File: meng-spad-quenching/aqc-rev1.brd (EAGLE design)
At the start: 127 x 88.9 mm, 137 parts, among them IC1 ADCMP582, IC2 NC7SV74K8X, IC3 LT3032-5, IC4 OPA342, IC5 OPA342, IC6 LTC1711, IC7 DS1100LU-20+, IC8 LT3032-15, IC9 NC7WZ16P6X, J1 VIN_LOGIC, M1 BSS806N, Q1 MMBTH81, Q2 MMBTH81, Q3 MMBTH81, Q4 MMBTH81, Q5 MMBTH81, Q6 MMBTH81, T1 MMBTH10, T2 MMBTH10, T3 MMBTH10, T4 MMBTH10, T5 MMBTH10, T6 MMBTH10, T7 MMBTH10, U1 SN65EPT21DGK, U2 TPS78233DDCT, U3 SN65EPT22DGK, X1 CONN_SPAD, X2 CONN_PHOTON_COUNTER, X3 CONN_FORCE_QUENCH, X4 CONN_VREF_ONE_SHOT_EXT, X5 CONN_VREF_DIAMOND_IBIAS_EXT, X6 CONN_VREF_CASCODE_IBIAS_EXT

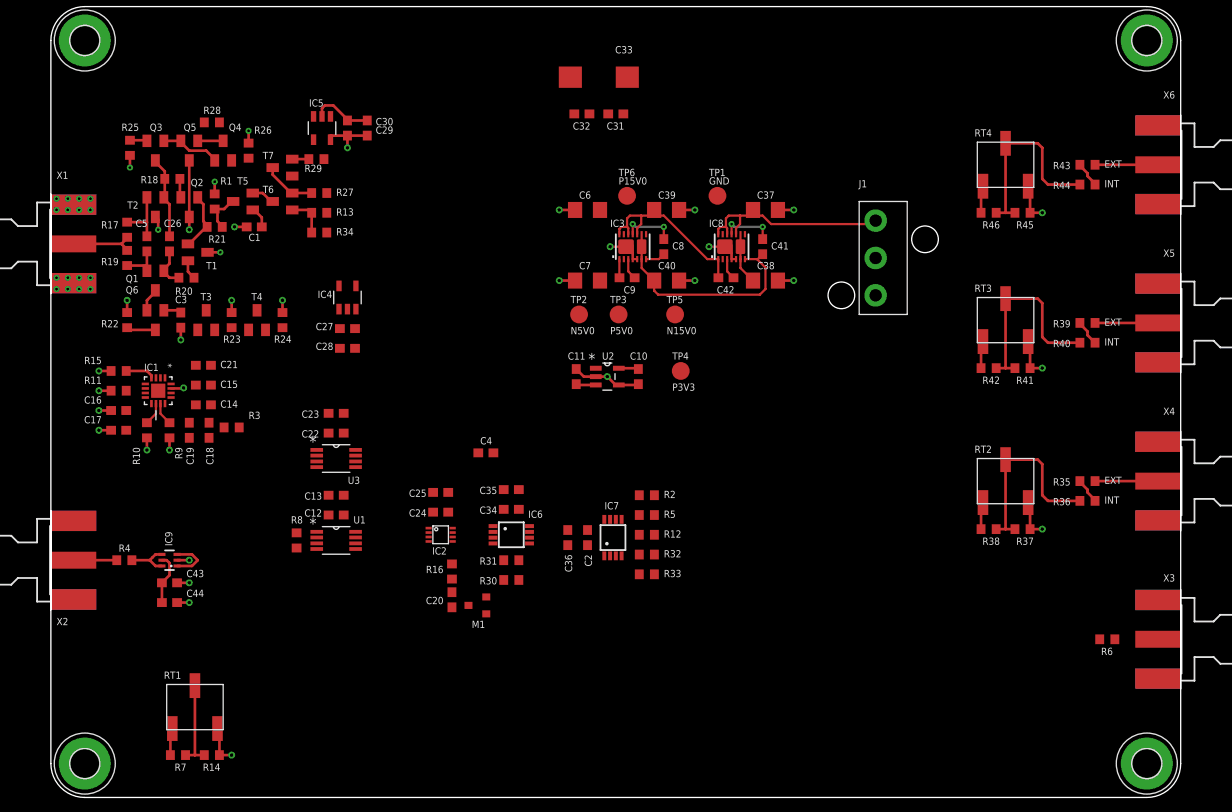
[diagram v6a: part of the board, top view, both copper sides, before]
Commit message: Worked on layout of CCS in AQC output stage
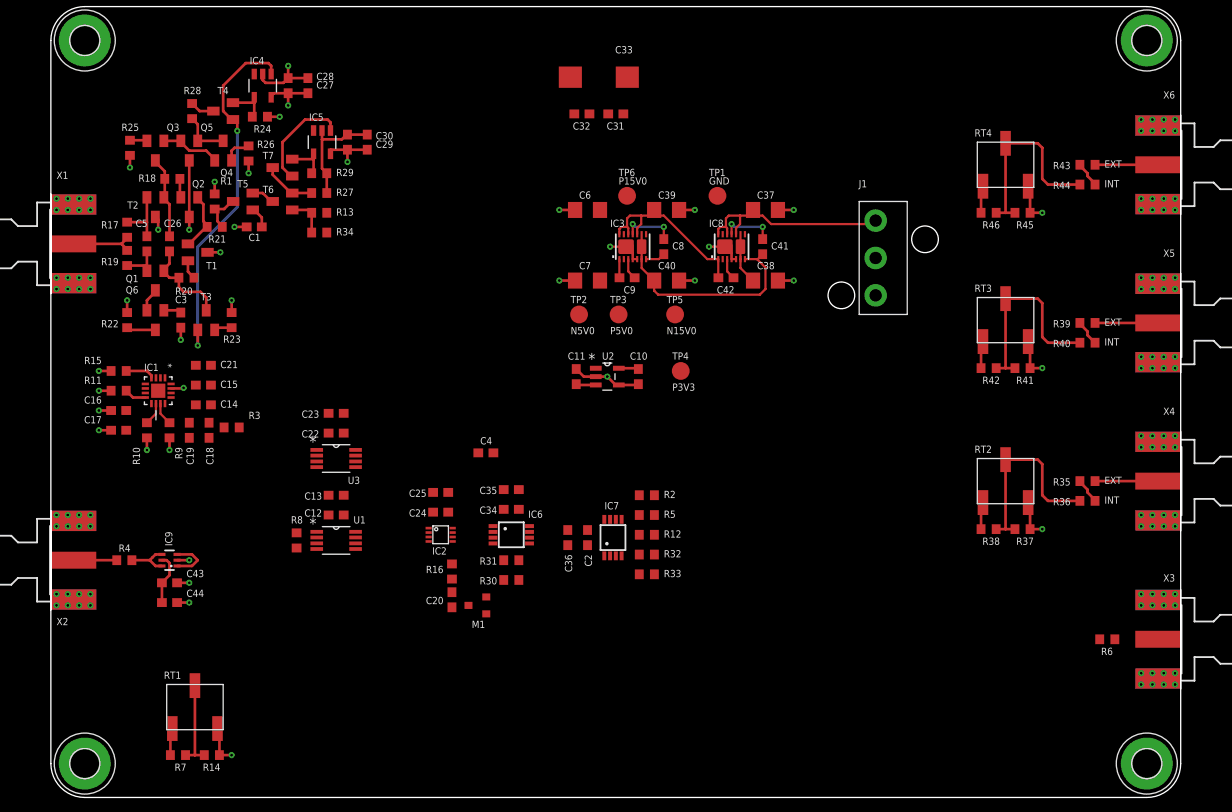
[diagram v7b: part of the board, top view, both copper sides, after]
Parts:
- moved C28 29.9 mm to (28.9, 80.0), turned to 90 degrees
- moved C27 28.1 mm to (26.7, 80.0), turned to 90 degrees
- moved IC4 25.6 mm to (23.8, 80.0), turned to 180 degrees
- moved T4 23.8 mm to (19.4, 77.2), turned to 90 degrees
- moved R24 23.0 mm to (23.5, 76.5), turned to 180 degrees
- moved R28 2.56 mm to (15.9, 77.2), turned to 270 degrees
- moved R29 1.62 mm to (30.2, 70.2)
- moved C29 1.59 mm to (33.3, 73.7)
- moved C30 1.59 mm to (35.6, 73.7)
- moved IC5 1.59 mm to (30.5, 73.7)
- moved R26 0.32 mm to (22.2, 72.4), turned to 270 degrees
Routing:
- net N$16: track 0.00 -> 41.2 mm, vias 0 -> 2
- net GND: track 81.2 -> 108.7 mm, vias 46 -> 127
- net N$30: track 0.00 -> 11.8 mm
- net N$19: track 4.54 -> 10.6 mm
- net PP_P5V0: track 14.9 -> 20.7 mm, vias 0 -> 1
- net PP_N5V0: track 9.11 -> 14.8 mm
- net N$23: track 0.00 -> 4.67 mm
- net N$29: track 0.00 -> 3.23 mm
- net N$35: track 1.86 -> 4.68 mm
- net N$18: track 2.86 -> 5.62 mm
- net N$27: track 0.00 -> 2.74 mm
- net N$6: track 0.00 -> 2.46 mm
- net N$20: track 0.00 -> 2.01 mm

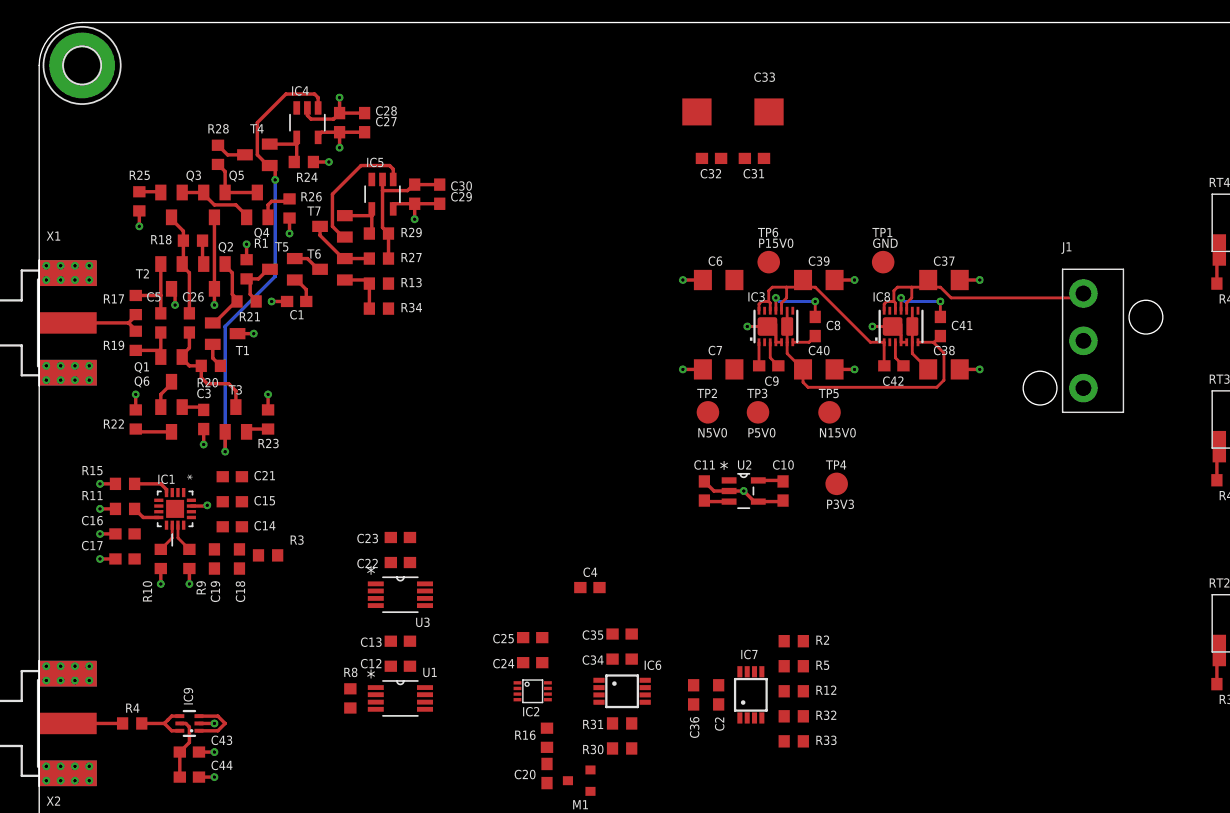
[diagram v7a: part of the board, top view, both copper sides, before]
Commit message: Switched low-voltage IC decoupling caps from 0603 to 0402
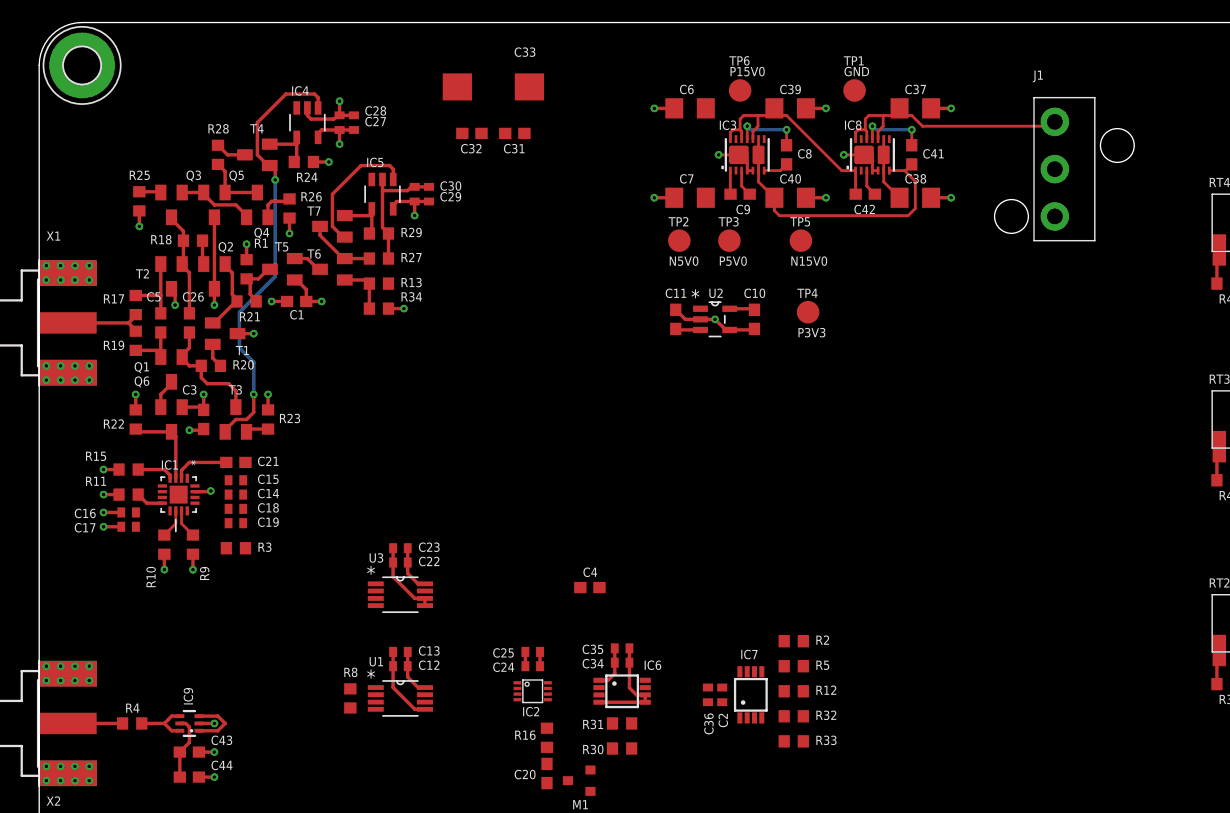
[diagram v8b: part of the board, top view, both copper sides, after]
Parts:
- C12, C13, C14, C15, C16, C17, C18, C19, C2, C22, C23, C24, C25, C27, C28, C29, C30, C34, C35, C36: device rcl:C0603 -> rcl:C0402
- moved C31 21.4 mm to (42.2, 79.1)
- moved C32 21.4 mm to (38.4, 79.1)
- moved C33 21.4 mm to (40.3, 83.2)
- moved TP1 15.5 mm to (72.4, 82.9)
- moved TP6 15.5 mm to (62.2, 82.9)
- moved C10 15.5 mm to (63.5, 62.5)
- moved C38 15.5 mm to (77.8, 73.3)
- moved C40 15.5 mm to (66.7, 73.3)
- moved C41 15.5 mm to (77.5, 77.2)
- moved C7 15.5 mm to (57.8, 73.3)
- moved TP5 15.5 mm to (67.6, 69.5)
- moved C11 15.5 mm to (56.5, 62.5)
- moved C8 15.5 mm to (66.4, 77.2)
- moved IC3 15.5 mm to (62.9, 77.2)
- moved IC8 15.5 mm to (74.0, 77.2)
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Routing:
- net GND: track 108.7 -> 132.9 mm, vias 127 -> 128
- net PP_P3V3: track 14.2 -> 27.6 mm
- net VREF_AV_DET: track 9.92 -> 14.9 mm
- net SPAD_PULLDN_SENSE: track 3.28 -> 7.56 mm
- net N$16: track 41.2 -> 39.2 mm
- net PP_P5V0: track 20.7 -> 22.6 mm, vias 1 -> 3
- net PP_N5V0: track 14.8 -> 13.9 mm
